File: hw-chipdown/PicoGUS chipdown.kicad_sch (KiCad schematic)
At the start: 55 parts, among them J1 Bus_ISA_8bit, J2 DEBUG, J3 IRQDMA_JP, J4 UART_TX, J5 USB_A - joy, J7 3.5mm TRS, J8 Wavetable, J9 3.5mm TRS, Q1 AO3401A, SW1 SW_Push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

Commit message: Almost final PicoGUS 2.0
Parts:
- removed C1: 0.1uF, Capacitor_SMD:C_0402_1005Metric, symbol Device:C
- added C2: 0.1uF, Capacitor_SMD:C_0402_1005Metric, symbol Device:C
- added C39, C40, C41, C42, C43, C44: 2.2uF, Capacitor_SMD:CP_Elec_4x5.4, symbol Device:C_Polarized_Small
- added FB4: 100Ω@100MHz, Inductor_SMD:L_0805_2012Metric, symbol Device:FerriteBead_Small
- added J10: Conn_01x02_Pin, Connector_PinHeader_2.54mm:PinHeader_1x02_P2.54mm_Vertical, symbol Connector:Conn_01x02_Pin
- FB1, FB2: value 1K@100MHz -> 1KΩ@100MHz
- R2, R3: footprint Resistor_SMD:R_0603_1608Metric -> Resistor_SMD:R_0805_2012Metric
- R6, R7, R8, R9: footprint Resistor_SMD:R_0603_1608Metric -> Resistor_SMD:R_0402_1005Metric
- U3: value 74HCT14 -> 74AHC14
- U6: value 74LVC2G07 -> 74LVC2G06
- U6: value 74LVC2G07 -> 74LVC2G06; symbol 74xGxx:74LVC2G07 -> 74xGxx:74LVC2G06
- renumbered C2 to C1
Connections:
- net +3V3: now also U6.5 (VCC), C2.1
- net +5V: no longer U6.5 (VCC)
- net GND: now also C2.2, J10.2 (Pin_2); no longer U4.12, U4.13
- net PGAUDIO_L: now also C43.1; no longer R9.2
- net PGAUDIO_R: now also C44.1; no longer R8.2
- net RUN: now also J10.1 (Pin_1)
- net UART_TX: now also U4.12, U4.13; no longer U6.1
- net WTAUDIO_L: now also C39.1; no longer U13.1 (1ch_IN)
- net WTAUDIO_R: now also C40.1; no longer U13.8 (2ch_IN)
- net at R7.1: now also C41.2; no longer U13.2 (1ch_OUT)
- net at U4.11: now also U6.1
- net at U13.7 (2ch_OUT): now also C42.1; no longer R6.1
- new net: C43.2, R9.2
- new net: C39.2, U13.1 (1ch_IN)
- new net: C44.2, R8.2
- new net: C41.1, U13.2 (1ch_OUT)
- new net: C40.2, U13.8 (2ch_IN)
- new net: C42.2, R6.1
- no-connect marks 34 -> 33
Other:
- moved on the sheet: C1, FB1, FB2, J7, J9, R2, R3, R6, R7, R8, R9, U4D

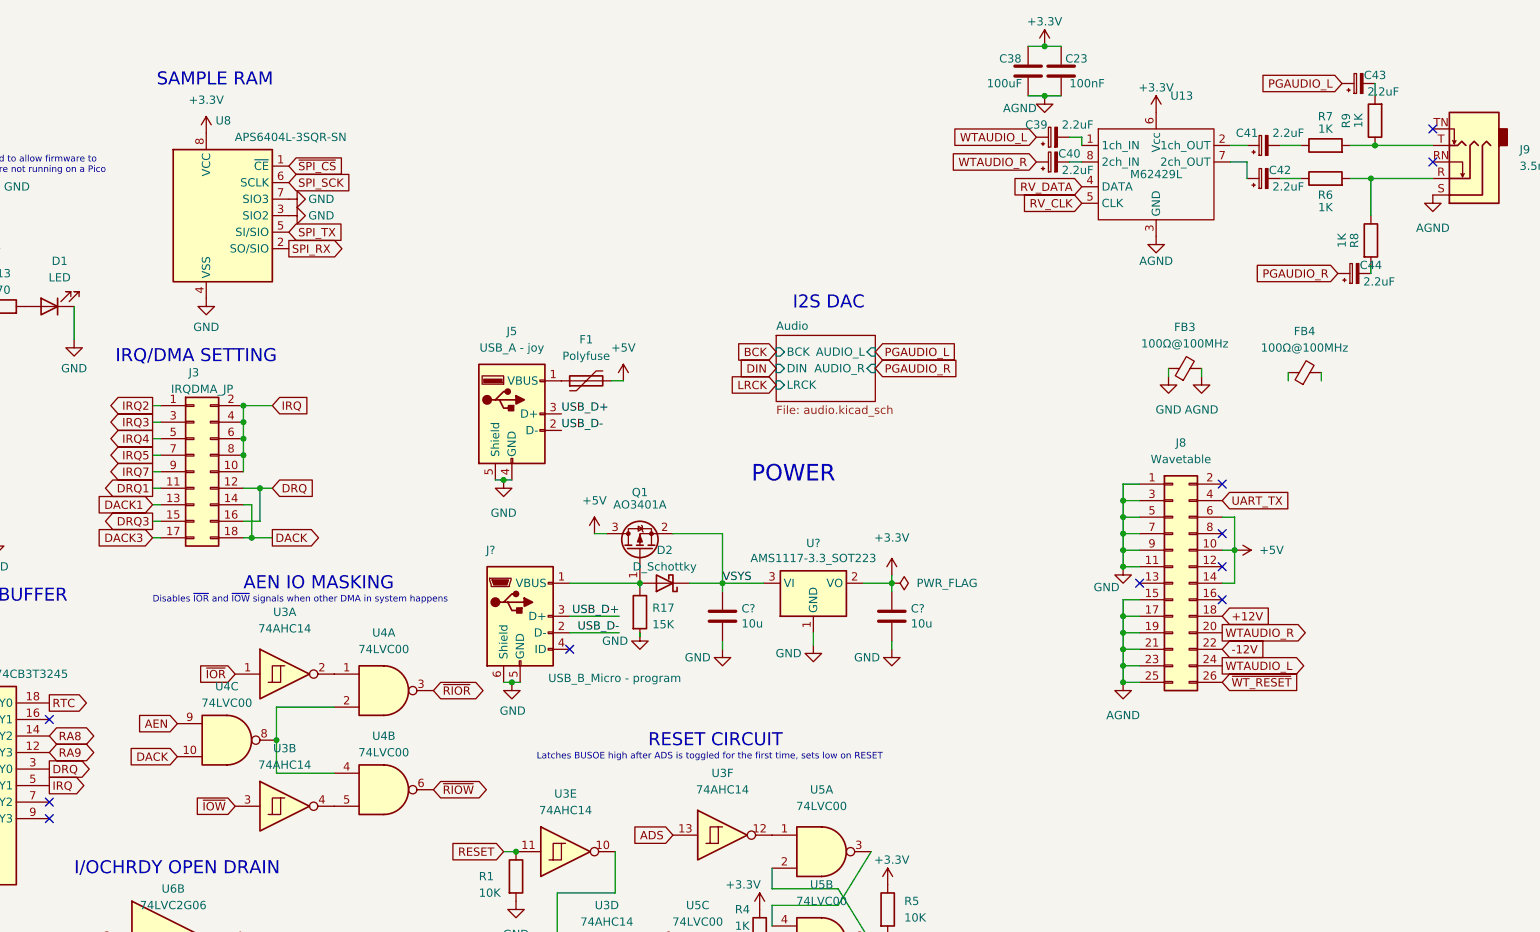
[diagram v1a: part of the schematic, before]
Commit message: PicoGUS v2.0 produced at JLCPCB 2023-10-23
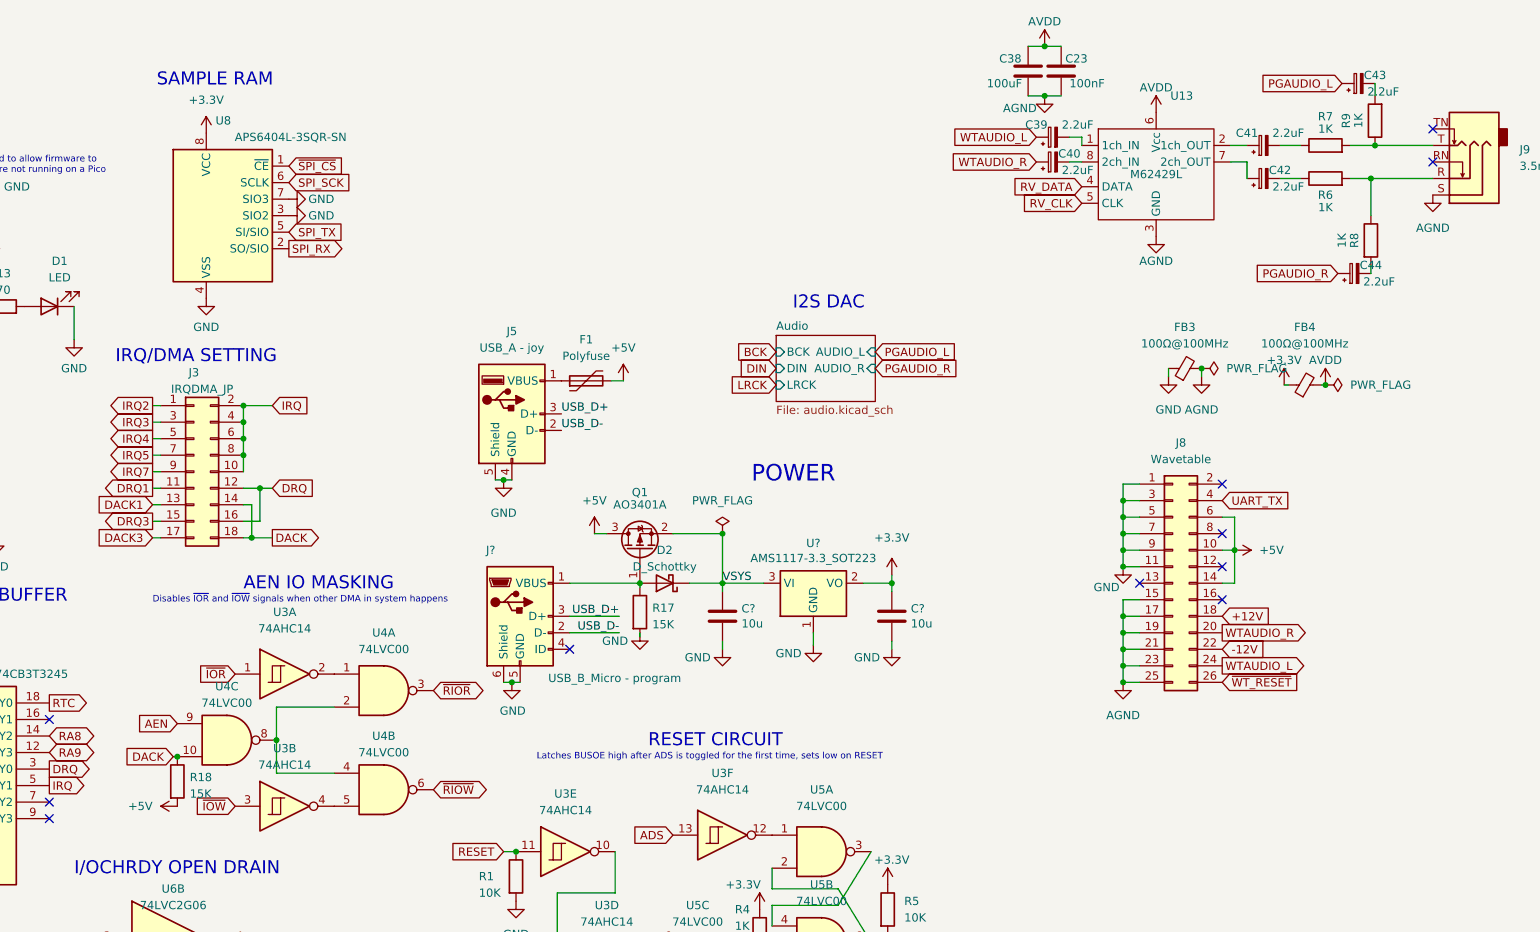
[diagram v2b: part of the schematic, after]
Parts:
- added R18: 15K, Resistor_SMD:R_0402_1005Metric, symbol Device:R
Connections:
- net +3V3: now also FB4.1; no longer C23.1, C38.1, U13.6 (Vcc)
- net +5V: now also R18.2
- net DACK: now also R18.1
- net AVDD: now reaches FB4.2
- net AVDD: now also C23.1, C38.1, U13.6 (Vcc)
- net GNDS renamed AGND
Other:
- moved on the sheet: FB4

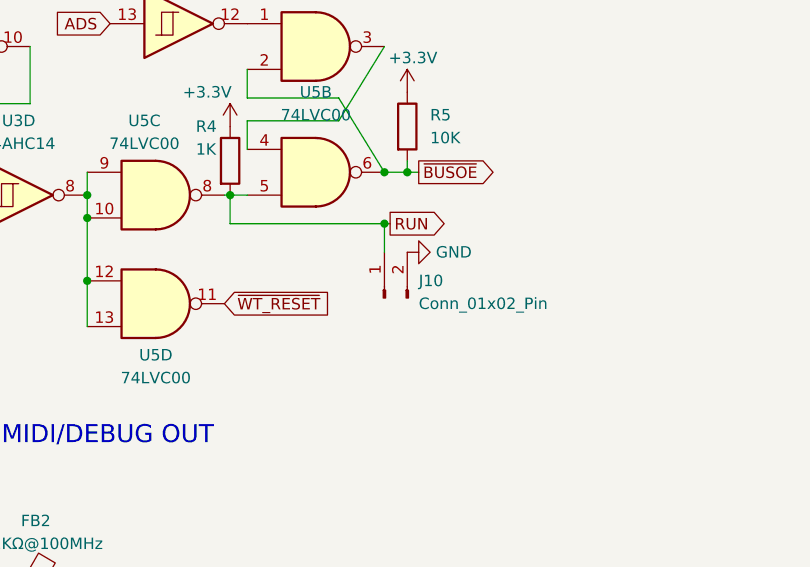
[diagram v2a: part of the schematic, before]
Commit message: PicoGUS v2.0 produced at JLCPCB 2023-10-24 - previous submission had awful errors
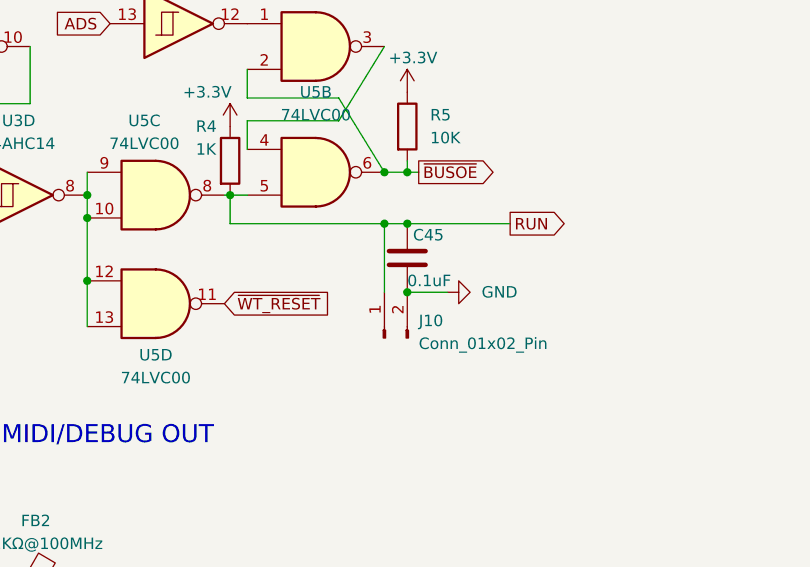
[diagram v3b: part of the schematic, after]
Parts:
- added C45: 0.1uF, Capacitor_SMD:C_0402_1005Metric, symbol Device:C
- H1, H2, J1, J10, J2, J4: now left out of the parts list
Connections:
- net GND: now also C45.2
- net RUN: now also C45.1
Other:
- moved on the sheet: J10
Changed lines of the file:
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@@
   (junction (at 47.625 182.88) (diameter 0) (color 0 0 0 0)
   )
+  (junction (at 274.32 161.29) (diameter 0) (color 0 0 0 0)
+  )
   (junction (at 310.515 92.71) (diameter 0) (color 0 0 0 0)
   )
@@
   (junction (at 62.865 182.88) (diameter 0) (color 0 0 0 0)
   )
+  (junction (at 274.32 168.91) (diameter 0) (color 0 0 0 0)
+  )
   (junction (at 310.515 90.17) (diameter 0) (color 0 0 0 0)
   )
@@
     (stroke (width 0) (type default))
   )
-  (wire (pts (xy 272.415 161.29) (xy 271.78 161.29))
+  (wire (pts (xy 285.75 161.29) (xy 274.32 161.29))
     (stroke (width 0) (type default))
   )
@@
     (stroke (width 0) (type default))
   )
-  (wire (pts (xy 271.78 161.29) (xy 254.635 161.29))
-    (stroke (width 0) (type default))
-  )
   (wire (pts (xy 295.91 17.78) (xy 298.45 17.78))
     (stroke (width 0) (type default))
@@
     (stroke (width 0) (type default))
   )
+  (wire (pts (xy 271.78 161.29) (xy 274.32 161.29))
+    (stroke (width 0) (type default))
+  )
   (wire (pts (xy 107.315 166.37) (xy 120.015 166.37))
     (stroke (width 0) (type default))
@@
     (stroke (width 0) (type default))
   )
-  (wire (pts (xy 271.78 161.29) (xy 271.78 164.465))
+  (wire (pts (xy 271.78 161.29) (xy 271.78 168.91))
     (stroke (width 0) (type default))
   )
@@
     (stroke (width 0) (type default))
   )
+  (wire (pts (xy 278.765 168.91) (xy 274.32 168.91))
+    (stroke (width 0) (type default))
+  )
   (wire (pts (xy 52.705 182.88) (xy 57.785 182.88))
     (stroke (width 0) (type default))
@@
     (stroke (width 0) (type default))
   )
+  (wire (pts (xy 254.635 161.29) (xy 271.78 161.29))
+    (stroke (width 0) (type default))
+  )
   (wire (pts (xy 177.8 90.805) (xy 175.26 90.805))
     (stroke (width 0) (type default))
@@
     )
   )
-  (global_label "RUN" (shape output) (at 272.415 161.29 0) (fields_autoplaced)
+  (global_label "RUN" (shape output) (at 285.75 161.29 0) (fields_autoplaced)
     (effects (font (size 1.27 1.27)) (justify left))
-    (property "Intersheetrefs" "${INTERSHEET_REFS}" (at 278.677 161.29 0)
+    (property "Intersheetrefs" "${INTERSHEET_REFS}" (at 292.012 161.29 0)
       (effects (font (size 1.27 1.27)) (justify left) hide)
     )
@@
     )
   )
+  (symbol (lib_id "Device:C") (at 274.32 165.1 0) (unit 1)
+    (in_bom yes) (on_board yes) (dnp no)
+    (property "Reference" "C45" (at 274.955 162.56 0)
+      (effects (font (size 1.27 1.27)) (justify left))
+    )
+    (property "Value" "0.1uF" (at 274.32 167.64 0)
+      (effects (font (size 1.27 1.27)) (justify left))
+    )
+    (property "Footprint" "Capacitor_SMD:C_0402_1005Metric" (at 275.2852 168.91 0)
+      (effects (font (size 1.27 1.27)) hide)
+    )
+    (property "Datasheet" "~" (at 274.32 165.1 0)
+      (effects (font (size 1.27 1.27)) hide)
+    )
+    (pin "1")
+    (pin "2")
+    (instances
+      (project "PicoGUS chipdown"
+        (path "/8fb4b197-630e-4faa-9892-8ecaeb71c13b"
+          (reference "C45") (unit 1)
+        )
+      )
+    )
+  )
   (symbol (lib_id "Device:C") (at 27.305 186.69 0) (unit 1)
     (in_bom yes) (on_board yes) (dnp no)
@@
     )
   )
+  (symbol (lib_id "power:GND") (at 278.765 168.91 90) (unit 1)
+    (in_bom yes) (on_board yes) (dnp no) (fields_autoplaced)
+    (property "Reference" "#PWR085" (at 285.115 168.91 0)
+      (effects (font (size 1.27 1.27)) hide)
+    )
+    (property "Value" "GND" (at 282.575 168.91 90)
+      (effects (font (size 1.27 1.27)) (justify right))
+    )
+    (property "Footprint" "" (at 278.765 168.91 0)
+      (effects (font (size 1.27 1.27)) hide)
+    )
+    (property "Datasheet" "" (at 278.765 168.91 0)
+      (effects (font (size 1.27 1.27)) hide)
+    )
+    (pin "1")
+    (instances
+      (project "PicoGUS chipdown"
+        (path "/8fb4b197-630e-4faa-9892-8ecaeb71c13b"
+          (reference "#PWR085") (unit 1)
+        )
+      )
+    )
+  )
   (symbol (lib_id "Device:C_Polarized_Small") (at 346.71 23.495 90) (unit 1)
     (in_bom yes) (on_board yes) (dnp no)
@@
     )
   )
-  (symbol (lib_id "Connector:Conn_01x02_Pin") (at 271.78 169.545 90) (unit 1)
-    (in_bom yes) (on_board yes) (dnp no) (fields_autoplaced)
-    (property "Reference" "J10" (at 275.59 167.64 90)
+  (symbol (lib_id "Connector:Conn_01x02_Pin") (at 271.78 173.99 90) (unit 1)
+    (in_bom no) (on_board yes) (dnp no) (fields_autoplaced)
+    (property "Reference" "J10" (at 275.59 172.085 90)
       (effects (font (size 1.27 1.27)) (justify right))
     )
-    (property "Value" "Conn_01x02_Pin" (at 275.59 170.18 90)
+    (property "Value" "Conn_01x02_Pin" (at 275.59 174.625 90)
       (effects (font (size 1.27 1.27)) (justify right))
     )
-    (property "Footprint" "Connector_PinHeader_2.54mm:PinHeader_1x02_P2.54mm_Vertical" (at 271.78 169.545 0)
+    (property "Footprint" "Connector_PinHeader_2.54mm:PinHeader_1x02_P2.54mm_Vertical" (at 271.78 173.99 0)
       (effects (font (size 1.27 1.27)) hide)
     )
-    (property "Datasheet" "~" (at 271.78 169.545 0)
+    (property "Datasheet" "~" (at 271.78 173.99 0)
       (effects (font (size 1.27 1.27)) hide)
     )
@@
   )
   (symbol (lib_id "Mechanical:MountingHole_Pad") (at 24.765 165.1 0) (unit 1)
-    (in_bom yes) (on_board yes) (dnp no)
+    (in_bom no) (on_board yes) (dnp no)
     (property "Reference" "H2" (at 27.305 162.5599 0)
       (effects (font (size 1.27 1.27)) (justify left))
@@
   )
   (symbol (lib_id "Mechanical:MountingHole_Pad") (at 24.765 158.75 0) (unit 1)
-    (in_bom yes) (on_board yes) (dnp no) (fields_autoplaced)
+    (in_bom no) (on_board yes) (dnp no) (fields_autoplaced)
     (property "Reference" "H1" (at 27.94 156.2099 0)
       (effects (font (size 1.27 1.27)) (justify left))
@@
   )
   (symbol (lib_id "Connector:Conn_01x02_Male") (at 175.26 196.85 270) (unit 1)
-    (in_bom yes) (on_board yes) (dnp no)
+    (in_bom no) (on_board yes) (dnp no)
     (property "Reference" "J4" (at 172.72 193.04 90)
       (effects (font (size 1.27 1.27)) (justify left))
@@
   )
   (symbol (lib_id "Connector_Generic:Conn_01x03") (at 86.36 94.615 180) (unit 1)
-    (in_bom yes) (on_board yes) (dnp no) (fields_autoplaced)
+    (in_bom no) (on_board yes) (dnp no) (fields_autoplaced)
     (property "Reference" "J2" (at 86.36 86.36 0)
       (effects (font (size 1.27 1.27)))
@@
     )
   )
-  (symbol (lib_id "power:GND") (at 274.32 164.465 90) (unit 1)
-    (in_bom yes) (on_board yes) (dnp no) (fields_autoplaced)
-    (property "Reference" "#PWR085" (at 280.67 164.465 0)
-      (effects (font (size 1.27 1.27)) hide)
-    )
-    (property "Value" "GND" (at 277.495 164.465 90)
-      (effects (font (size 1.27 1.27)) (justify right))
-    )
-    (property "Footprint" "" (at 274.32 164.465 0)
-      (effects (font (size 1.27 1.27)) hide)
-    )
-    (property "Datasheet" "" (at 274.32 164.465 0)
-      (effects (font (size 1.27 1.27)) hide)
-    )
-    (pin "1")
-    (instances
-      (project "PicoGUS chipdown"
-        (path "/8fb4b197-630e-4faa-9892-8ecaeb71c13b"
-          (reference "#PWR085") (unit 1)
-        )
-      )
-    )
-  )
   (symbol (lib_id "power:+3.3V") (at 169.545 31.115 0) (unit 1)
     (in_bom yes) (on_board yes) (dnp no)
@@
   )
   (symbol (lib_id "Connector:Bus_ISA_8bit") (at 46.355 62.23 0) (unit 1)
-    (in_bom yes) (on_board yes) (dnp no) (fields_autoplaced)
+    (in_bom no) (on_board yes) (dnp no) (fields_autoplaced)
     (property "Reference" "J1" (at 46.355 16.51 0)
       (effects (font (size 1.27 1.27)))
